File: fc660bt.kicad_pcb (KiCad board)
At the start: 2 copper layers, 98 x 35 mm, 47 parts, among them J1 USB_B_Mini, J10 SWDIO, J11 FCTRYRST, J12 DFU, J13 VCC, J14 VBAT, J2 Conn_01x20, J3 Conn_01x02, J4 ICSP, J5 GND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

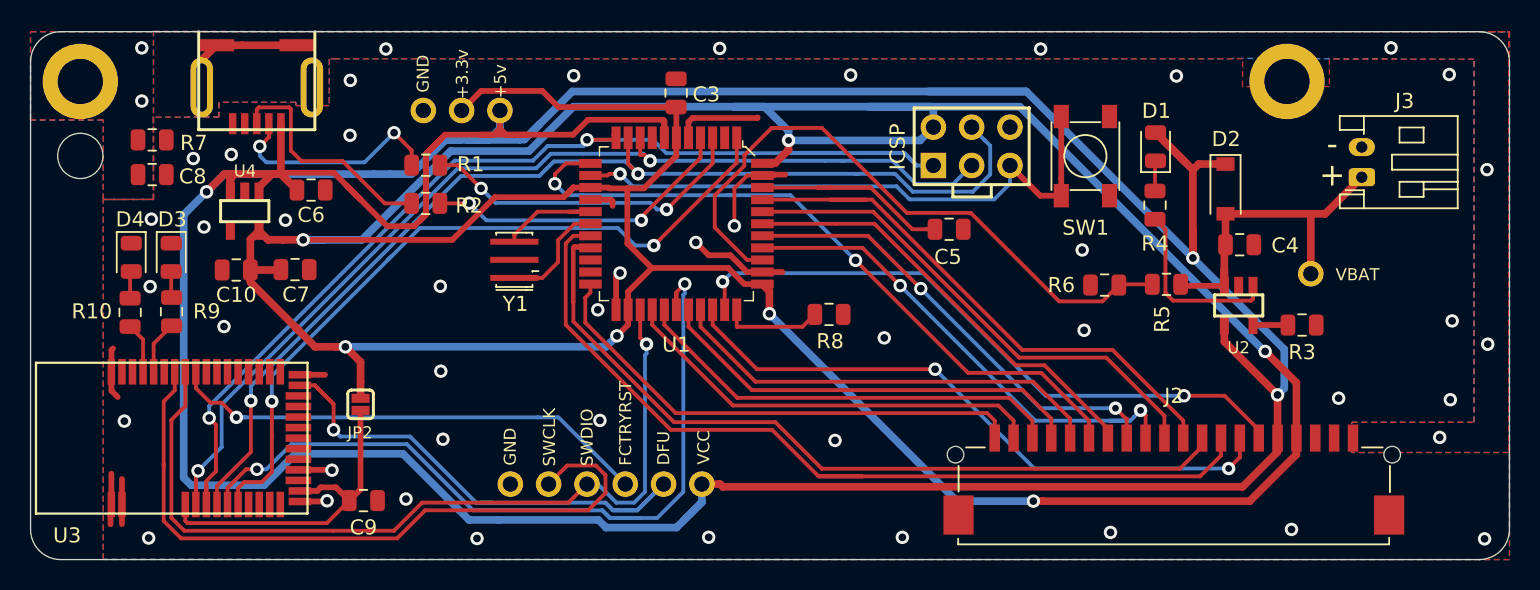
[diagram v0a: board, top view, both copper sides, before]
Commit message: Cleaned up and added comments to schematic
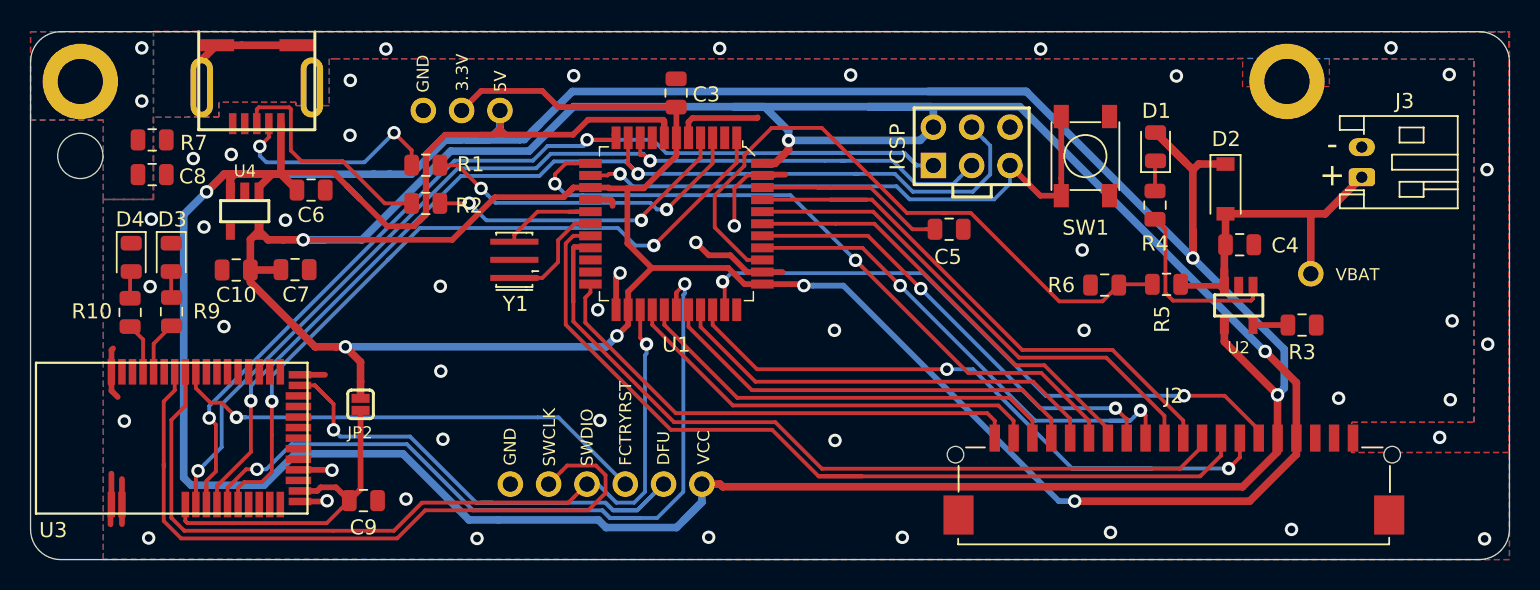
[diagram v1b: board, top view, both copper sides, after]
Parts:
- removed R8: 1K, Resistor_SMD:R_0805_2012Metric
- J3: value Conn_01x02 -> JST_PH
- J7: value +5v -> 5V
- J8: value +3.3v -> 3.3V
- SW1: value SW_Push -> RESET
- U3: footprint RF_Modules:MDBT40 -> fc660bt:MDBT40
- Y1: value Resonator -> 8MHz
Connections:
- U1 pad 33: Net-(R8-Pad2) -> GND
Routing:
- net Net-(R8-Pad2): track 6.65 -> 0.00 mm
- net /~OUT: track 41.5 -> 46.7 mm
- net +3V3: track 259.1 -> 256.1 mm

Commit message: Added switch to connect and disconnect battery
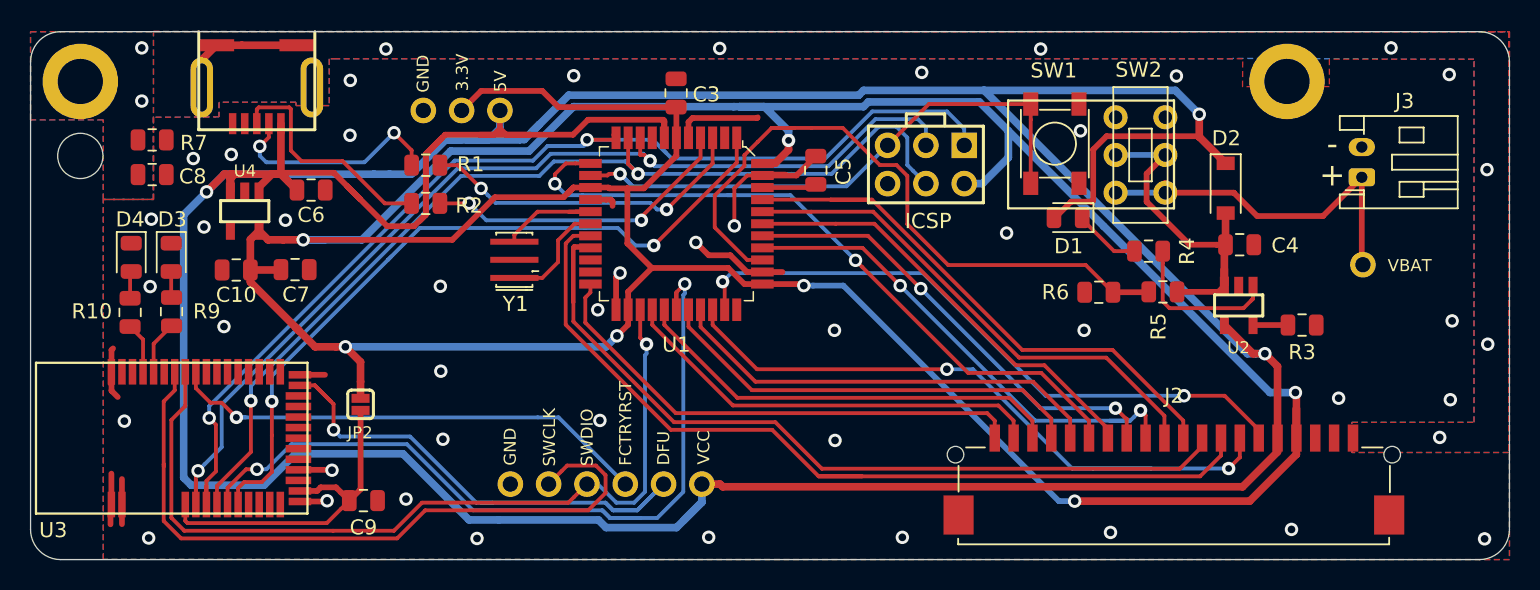
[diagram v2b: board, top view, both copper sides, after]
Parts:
- added SW2: SW_DPDT_x2, fc660bt:JS202011CQN, F.Cu at (106.5, 33.1)
- moved C5 9.67 mm to (85.0, 34.1), turned to 90 degrees
- moved D1 7.47 mm to (101.7, 37.3), turned to 180 degrees
- moved J14 3.51 mm to (121.2, 40.4)
- moved J4 3.27 mm to (92.3, 33.7), turned to 180 degrees
- moved R4 3.08 mm to (107.0, 39.5), turned to 180 degrees
- moved SW1 2.19 mm to (100.8, 32.4)
- moved R6 0.61 mm to (103.7, 42.2)
- moved R5 0.55 mm to (108.0, 42.2)
- moved D2 0.05 mm to (112.1, 35.3)
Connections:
- J14 pad 1: VBAT -> /BAT_RAW
- J3 pad 1: VBAT -> /BAT_RAW
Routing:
- net /BAT_RAW: track 0.00 -> 24.5 mm
- net /AREF: track 16.7 -> 7.29 mm
- net +3V3: track 256.1 -> 247.4 mm
- net VBUS: track 291.2 -> 297.6 mm
- net /MOSI: track 74.5 -> 69.4 mm
- net /MISO: track 80.6 -> 75.7 mm
- net GND: track 37.1 -> 41.2 mm, vias 39 -> 40
- net Net-(D1-Pad1): track 2.01 -> 4.94 mm
- net /SCK: track 70.9 -> 69.4 mm
- net /RST: track 39.7 -> 38.3 mm
- net Net-(R4-Pad1): track 12.1 -> 10.8 mm
- net /BAT_SENS: track 44.5 -> 45.1 mm
